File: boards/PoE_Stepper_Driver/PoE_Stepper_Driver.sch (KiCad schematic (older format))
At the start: 15 parts, among them U3 STM32F407VETx, U4 NCP1117, U5 12V DC/DC, Y1 8MHz

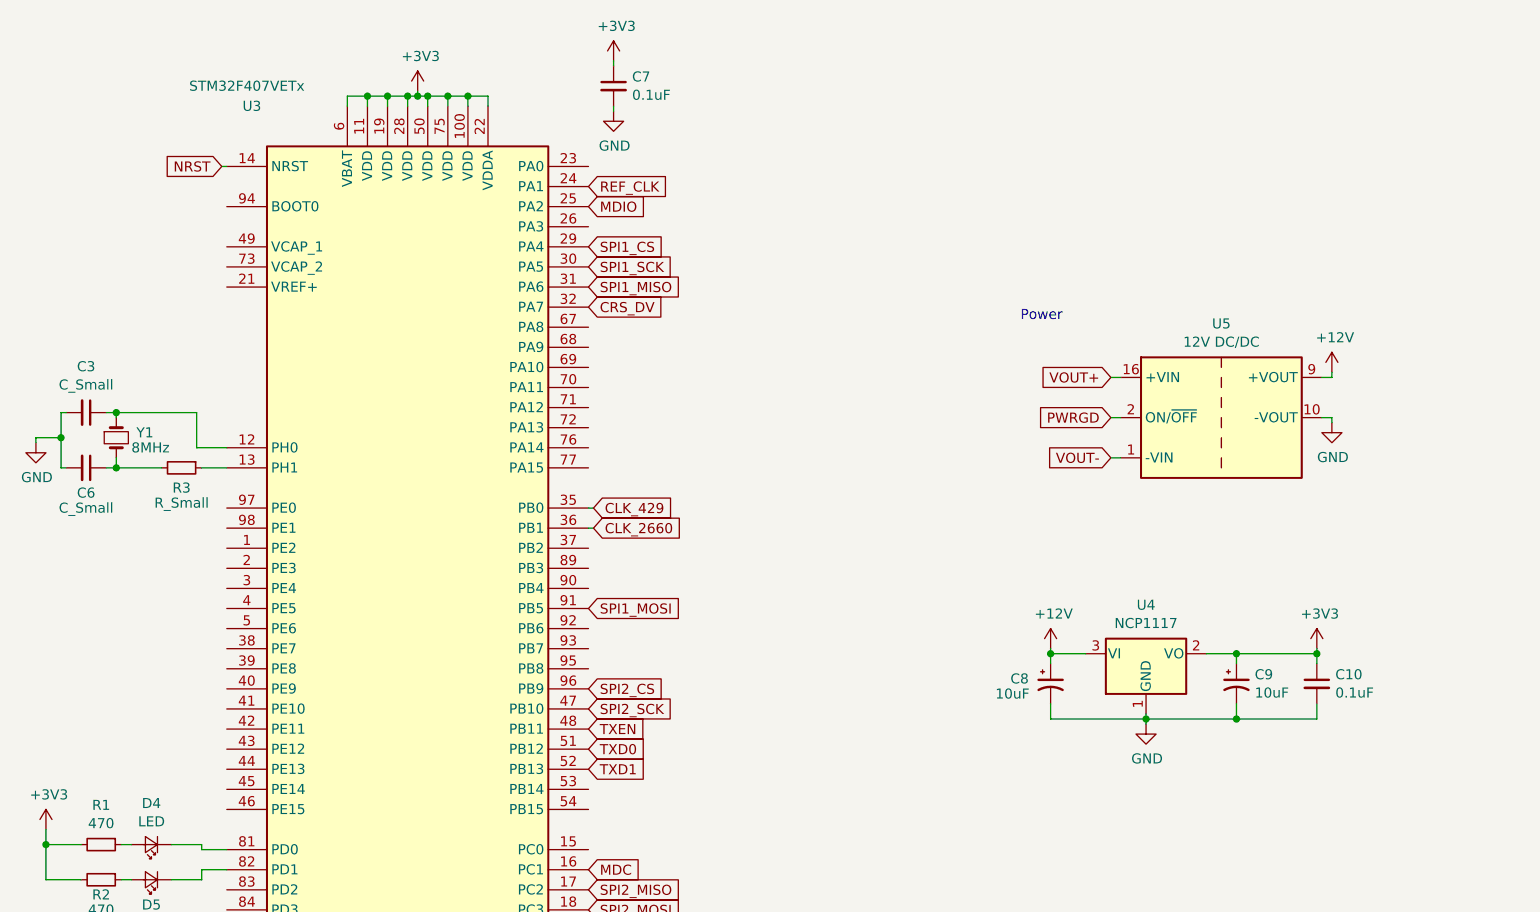
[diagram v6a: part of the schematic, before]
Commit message: added dp83848 phy and more caps
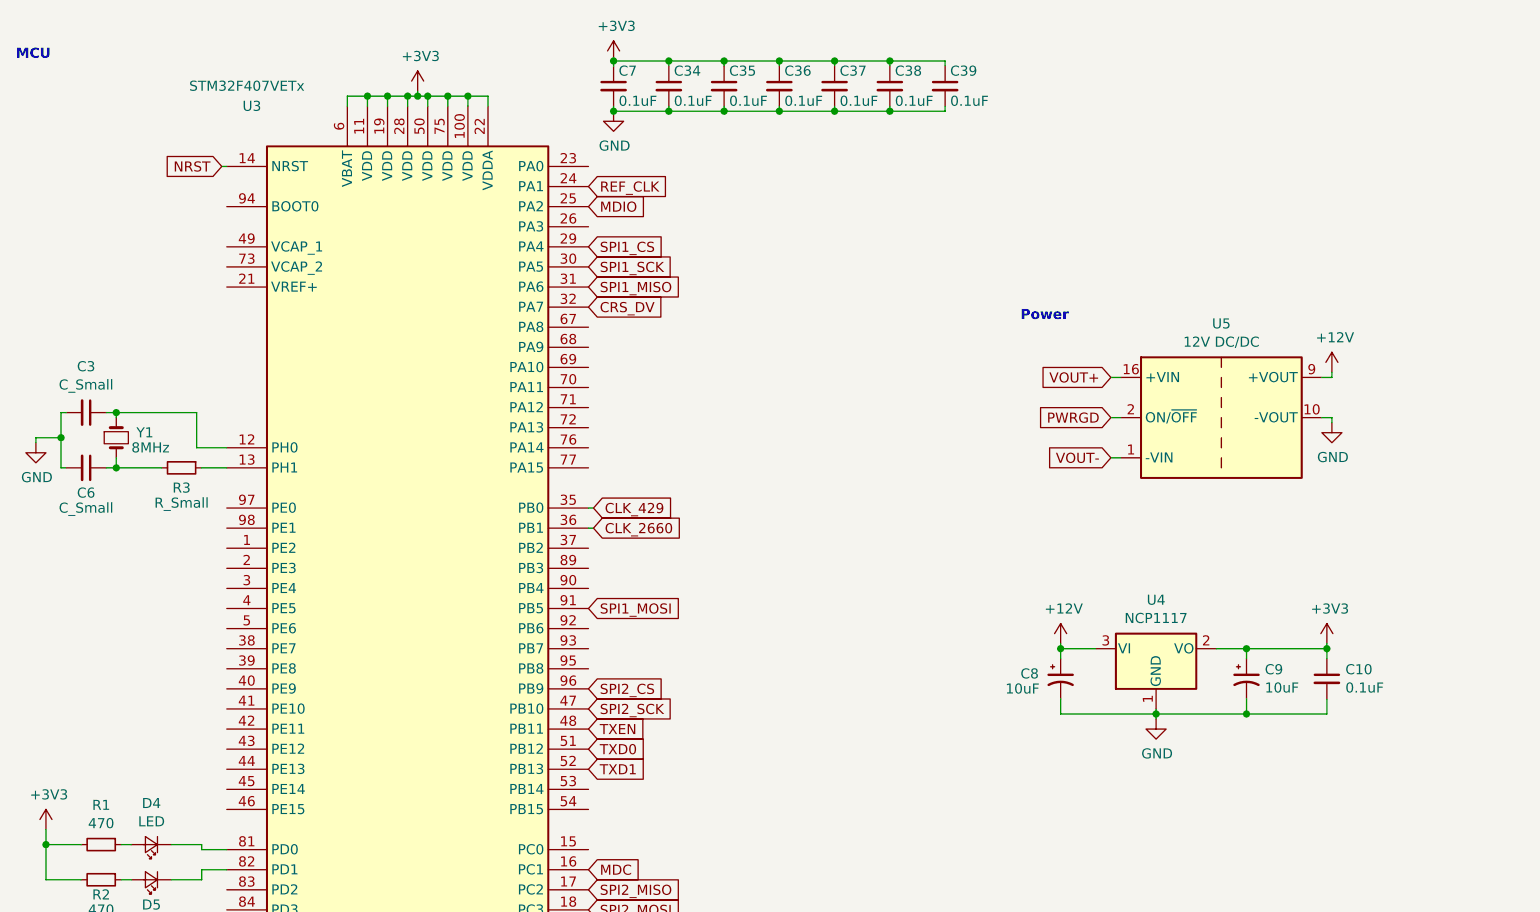
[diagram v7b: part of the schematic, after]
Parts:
- added C34, C35, C36, C37, C38, C39: 0.1uF, symbol device:C_Small
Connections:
- net +3V3: now also C34.1, C35.1, C36.1, C37.1, C38.1, C39.1
- net GND: now also C34.2, C35.2, C36.2, C37.2, C38.2, C39.2
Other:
- note added: "MCU"
- moved on the sheet: C10, C8, C9, U4

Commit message: started board layout
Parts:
- removed U5: 12V DC/DC, Converter_DCDC:Converter_DCDC_Artesyn_ATA_SMD, symbol Converter_DCDC:ATA00A18S-L
- added C40: 2.2uF, symbol device:C_Small
- added C41, C42: 2.2nF, symbol device:C_Small
- added C43: 100uF, symbol device:CP1_Small
- added FL1: 1.32mH, symbol device:EMI_Filter_CommonMode
- added R37: 10k, symbol device:R_Small
- added SW3: SW_Push, Button_Switch_SMD:SW_SPST_B3S-1000, symbol Switch:SW_Push
- added U5: E48SC12010, PoE_Stepper_Driver:E48SC12010, symbol ECE445:E48SC12010
- C10, C34, C35, C36, C37, C38, C39, C7: footprint (none) -> Capacitor_SMD:C_0805_2012Metric_Pad1.15x1.40mm_HandSolder
- D4, D5: footprint (none) -> LED_SMD:LED_0805_2012Metric_Pad1.15x1.40mm_HandSolder
- Y1: footprint (none) -> Crystal:Crystal_HC49-4H_Vertical
- renumbered C3 to C12
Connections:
- net +12V: now also U5.7 (Sense+), U5.8 (Vout+)
- net +3V3: now also R37.1
- net GND: now also C41.2, C42.1, SW3.2, U5.4 (Vout-), U5.5 (Sense-)
- net NRST: now also R37.2, SW3.1
- net PWRGD: now also U5.2 (ON/OFF)
- net VOUT+: now also C40.1, FL1.1
- net VOUT-: now also C40.2, FL1.3
- net REF_CLK: no longer names the net of U3.24 (PA1)
- new net: C41.1, C43.1, FL1.2, U5.1 (Vin+)
- new net: C42.2, C43.2, FL1.4, U5.3 (Vin-)
- no-connect marks 0 -> 65
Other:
- moved on the sheet: C10, C34, C35, C36, C37, C38, C39, C7, C8, C9, U4
